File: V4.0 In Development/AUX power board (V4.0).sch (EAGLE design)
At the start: 91 parts, among them U1 ATMEGA328P_TQFP, U2 TPS5405DR

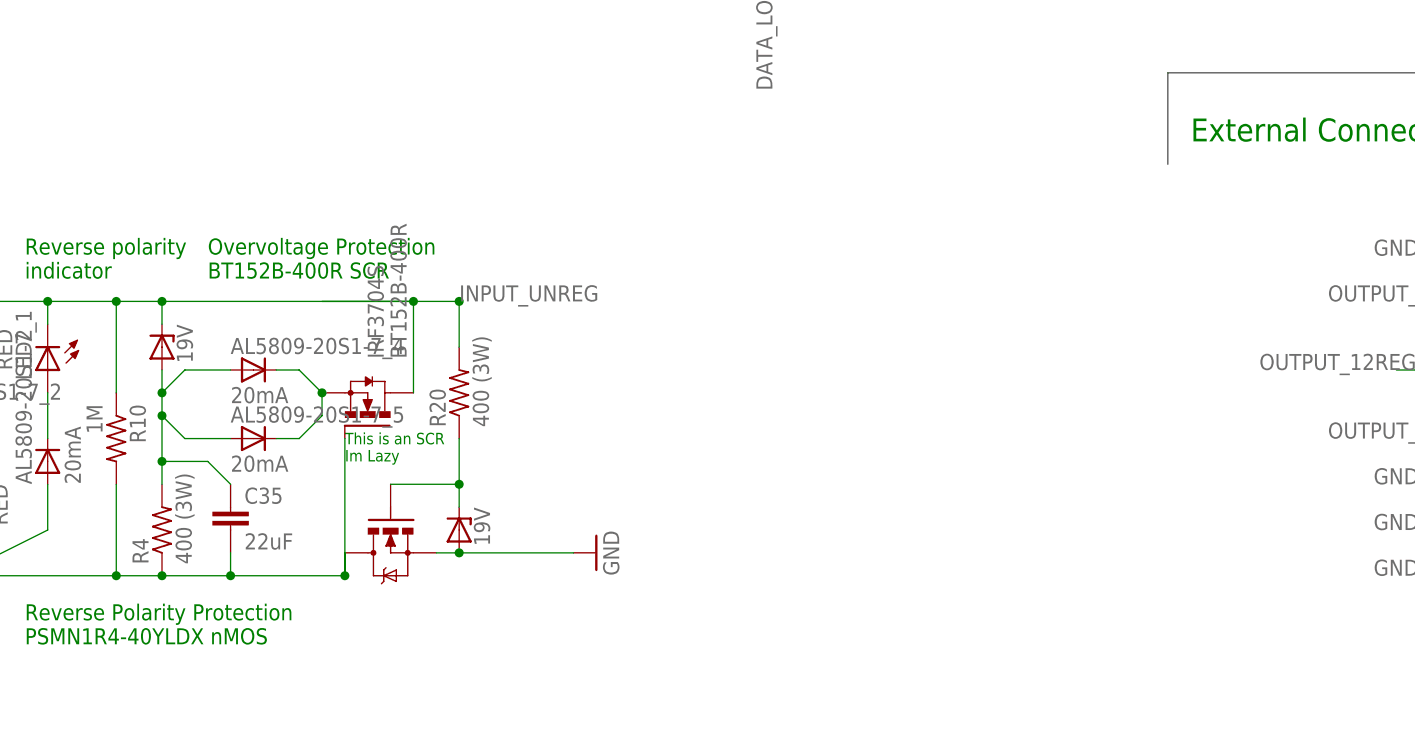
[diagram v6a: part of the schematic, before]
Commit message: Made some tweaks
Changed some values in the power protection circuit
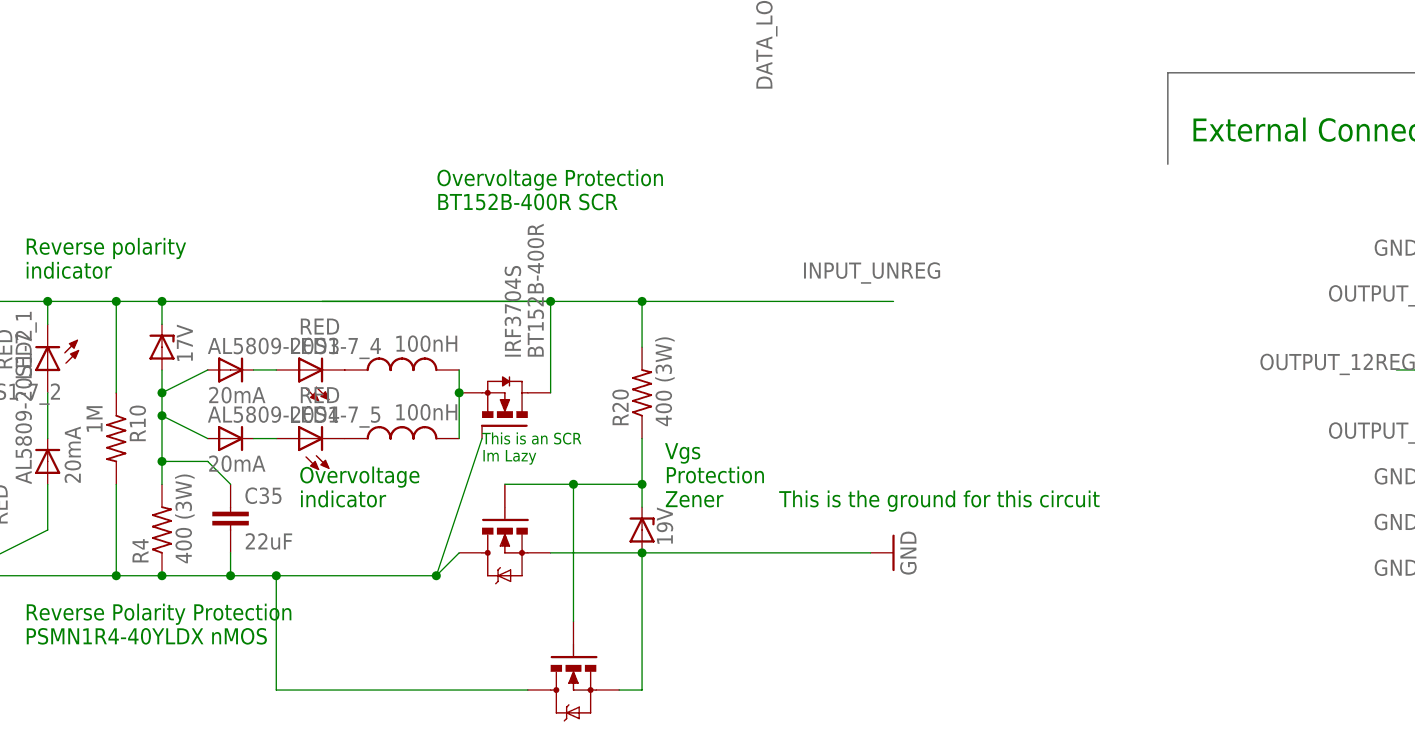
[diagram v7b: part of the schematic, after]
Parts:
- added LED3, LED4: RED, E-P-008-R1.2:LEDSML1206
- added MLZ2012DR10DT001, MLZ2012DR10DT002: 100nH, resistor:L-USL2012C
- added PSMN1R4-40TLDX2: MOSFET-NCHANNELFDS6630A, PSMN1R4-40YLDX:MOSFET-NCHANNELFDS6630A
- 1N5354BRLG: value 19V -> 17V
- renumbered 1N5356BRLG_2 to 1N5354BRLG
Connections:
- new net N$28: AL5809-20S1-7_4.C, LED3.A
- new net N$31: AL5809-20S1-7_5.C, LED4.A
- new net N$32: LED4.C, MLZ2012DR10DT002.1
- new net N$33: BT152B-400R.S, MLZ2012DR10DT001.2, MLZ2012DR10DT002.2
- net GND: now also PSMN1R4-40TLDX2.S
- net N$19: now also PSMN1R4-40TLDX2.G
- net N$30: now also LED3.C, MLZ2012DR10DT001.1; no longer AL5809-20S1-7_4.C, AL5809-20S1-7_5.C, BT152B-400R.S
- net NEG_TERMINAL: now also PSMN1R4-40TLDX2.D
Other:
- note added: "Overvoltage indicator"
- note added: "This is the ground for this circuit"
- note added: "Vgs Protection Zener"
- moved on the sheet: AL5809-20S1-7_4, AL5809-20S1-7_5, BT152B-400R, R20

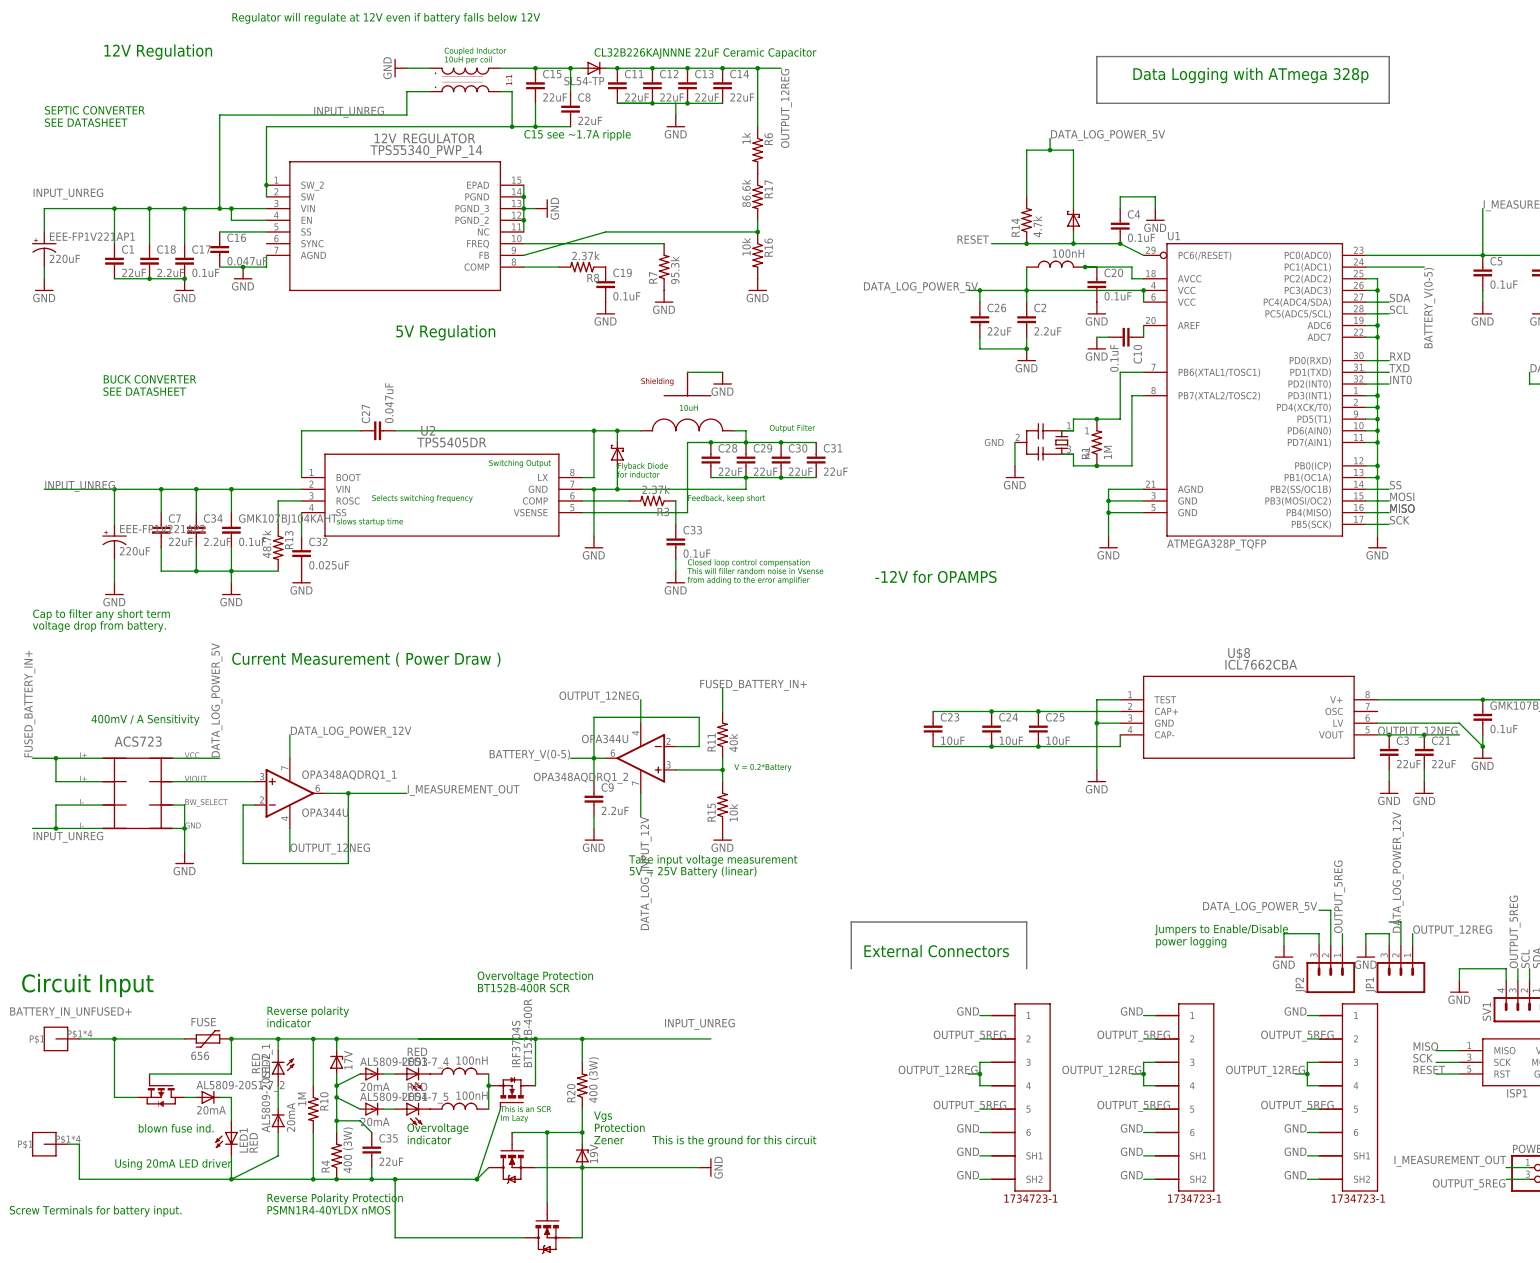
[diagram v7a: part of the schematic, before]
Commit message: Bunch of tweaks to lower cost and posted the parts list
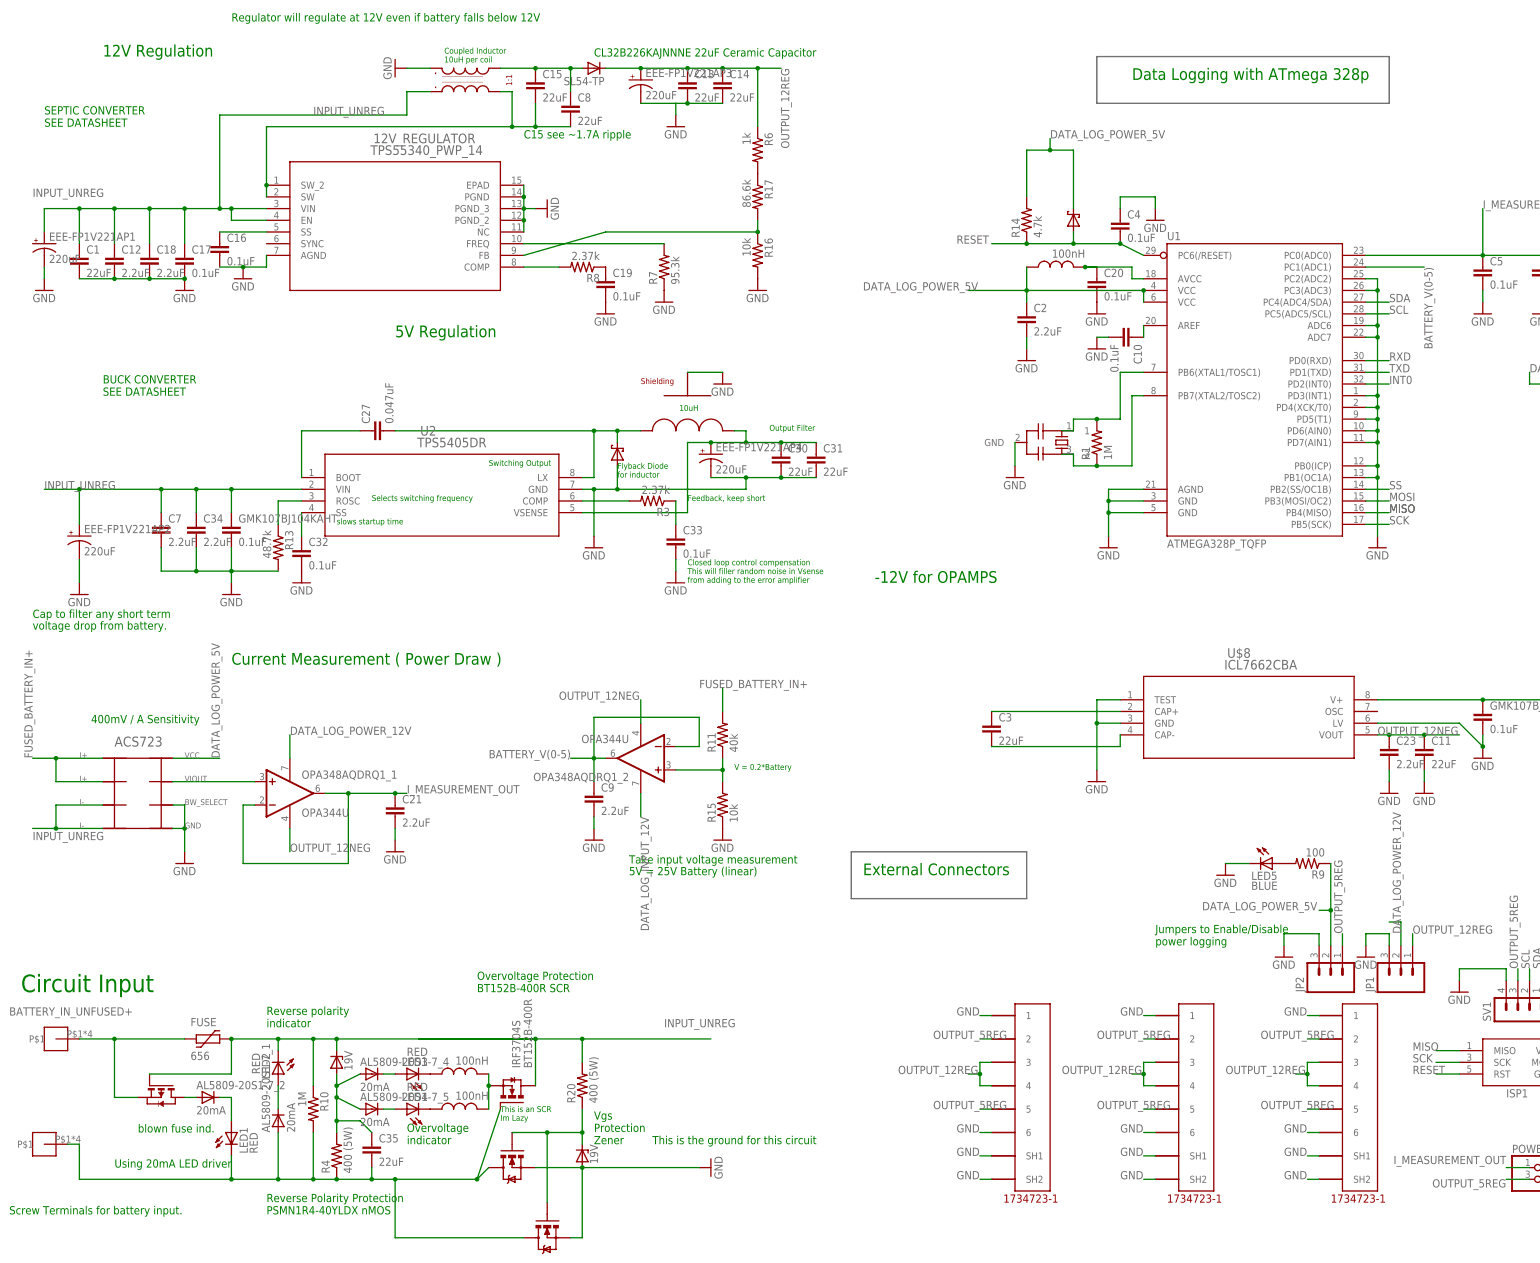
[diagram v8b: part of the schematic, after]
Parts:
- removed C24, C25: 10uF, rcl:C-EUC0805
- removed C26, C28, C29: 22uF, rcl:C-EUC1210
- added EEE-FP1V221AP3, EEE-FP1V221AP4: 220uF, rcl:CPOL-US175TMP-0808
- added LED5: BLUE, E-P-008-R1.2:LEDSML1206
- added R9: 100, rcl:R-US_R0805
- 1N5354BRLG: value 17V -> 19V
- C12, C21, C7: value 22uF -> 2.2uF; device rcl:C-EUC1210 -> rcl:C-EUC0603
- C16: value 0.047uF -> 0.1uF
- C23: value 10uF -> 2.2uF; device rcl:C-EUC0805 -> rcl:C-EUC0603
- C32: value 0.025uF -> 0.1uF
- R20, R4: value 400 (3W) -> 400 (5W); device resistor:R-US_R2512 -> resistor:R-US_0817/22
- renumbered PSMN1R4-40TLDX1 to PSMN1R4-40YLDX1, PSMN1R4-40TLDX2 to PSMN1R4-40YLDX2
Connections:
- new net N$34: LED5.A, R9.2
- net DATA_LOG_POWER_5V: now also R9.1; no longer C26.1
- net GND: now also EEE-FP1V221AP3.-, EEE-FP1V221AP4.-, LED5.C; no longer C26.2, C28.2, C29.2, C3.2
- net INPUT_UNREG: now also C12.1
- net I_MEASUREMENT_OUT: now also C21.1
- net N$11: now also C3.2; no longer C23.2, C24.2, C25.2
- net N$16: now also C3.1; no longer C23.1, C24.1, C25.1
- net N$26: now also EEE-FP1V221AP4.+; no longer C28.1, C29.1
- net OUTPUT_12NEG: now also C11.1, C23.1; no longer C21.1, C3.1
- net OUTPUT_12REG: now also EEE-FP1V221AP3.+; no longer C11.1, C12.1
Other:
- moved on the sheet: C1, C11, C12, C21, C23, C3, EEE-FP1V221AP2
